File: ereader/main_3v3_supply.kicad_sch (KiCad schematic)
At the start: 20 parts, among them Q3 DMN2056U-7, U13 TPS63806YFFR, U16 74LVC1G17GW,125

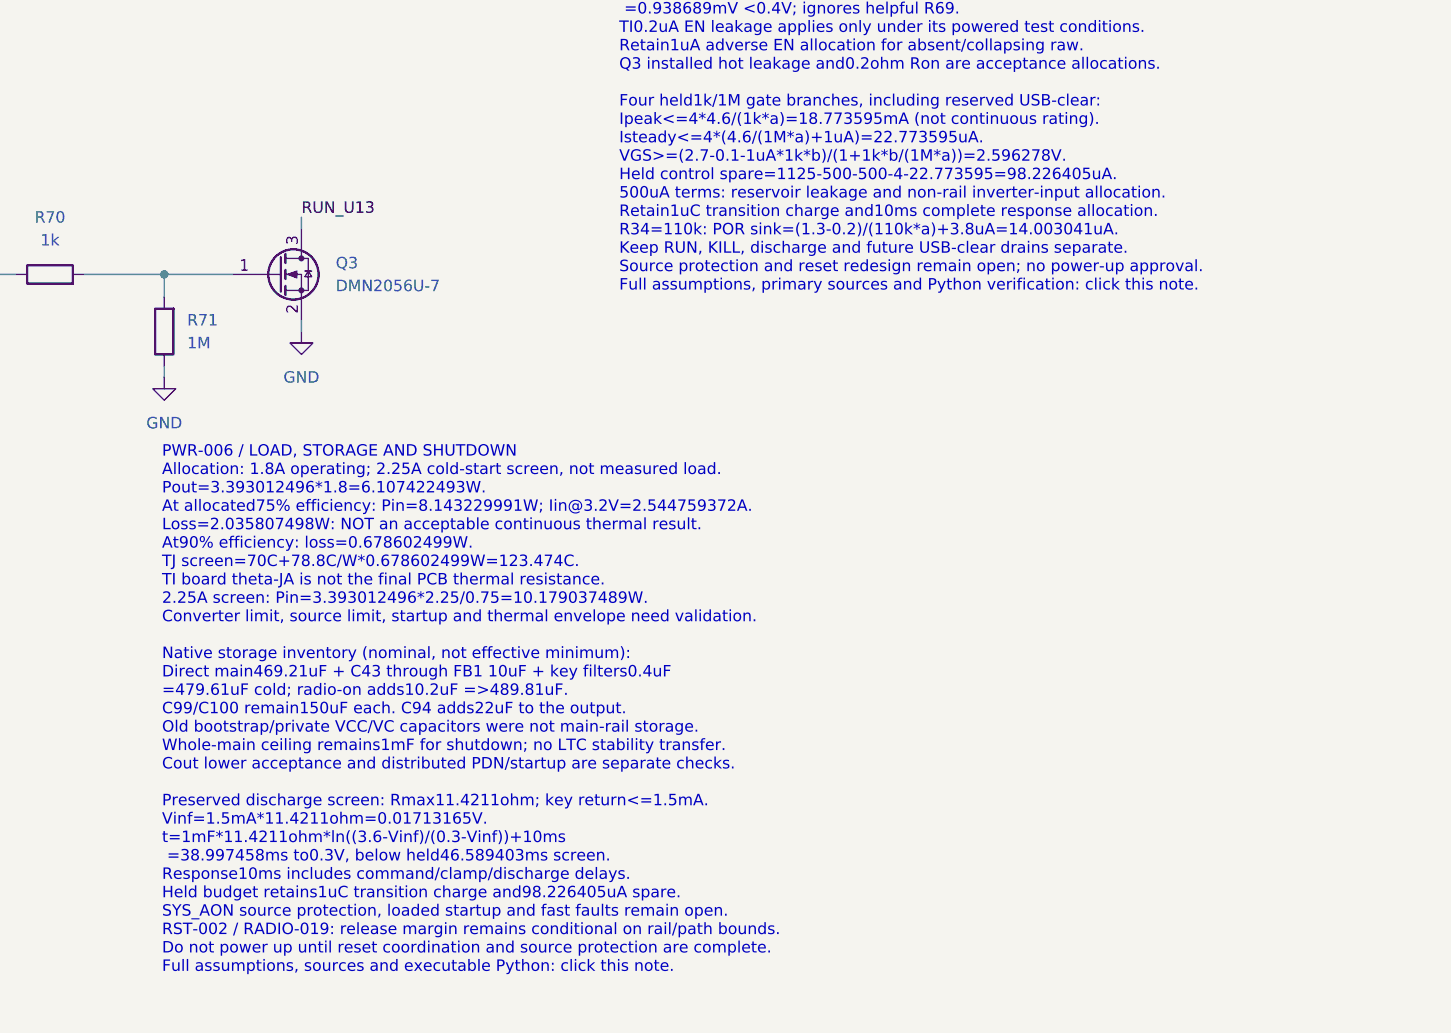
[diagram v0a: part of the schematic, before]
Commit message: WIP: integrate orientation sensor and refresh schematic review exports
Add LIS2DW12 host wiring and sourced passives, revise held-supply discharge calculations, document camera and capacitance screens, and refresh standard capacitor caches. Include reviewed 14-page PDF and reconciled native BOM. ERC remains 111 errors and 11 warnings; electrical design is incomplete. Refs #21.
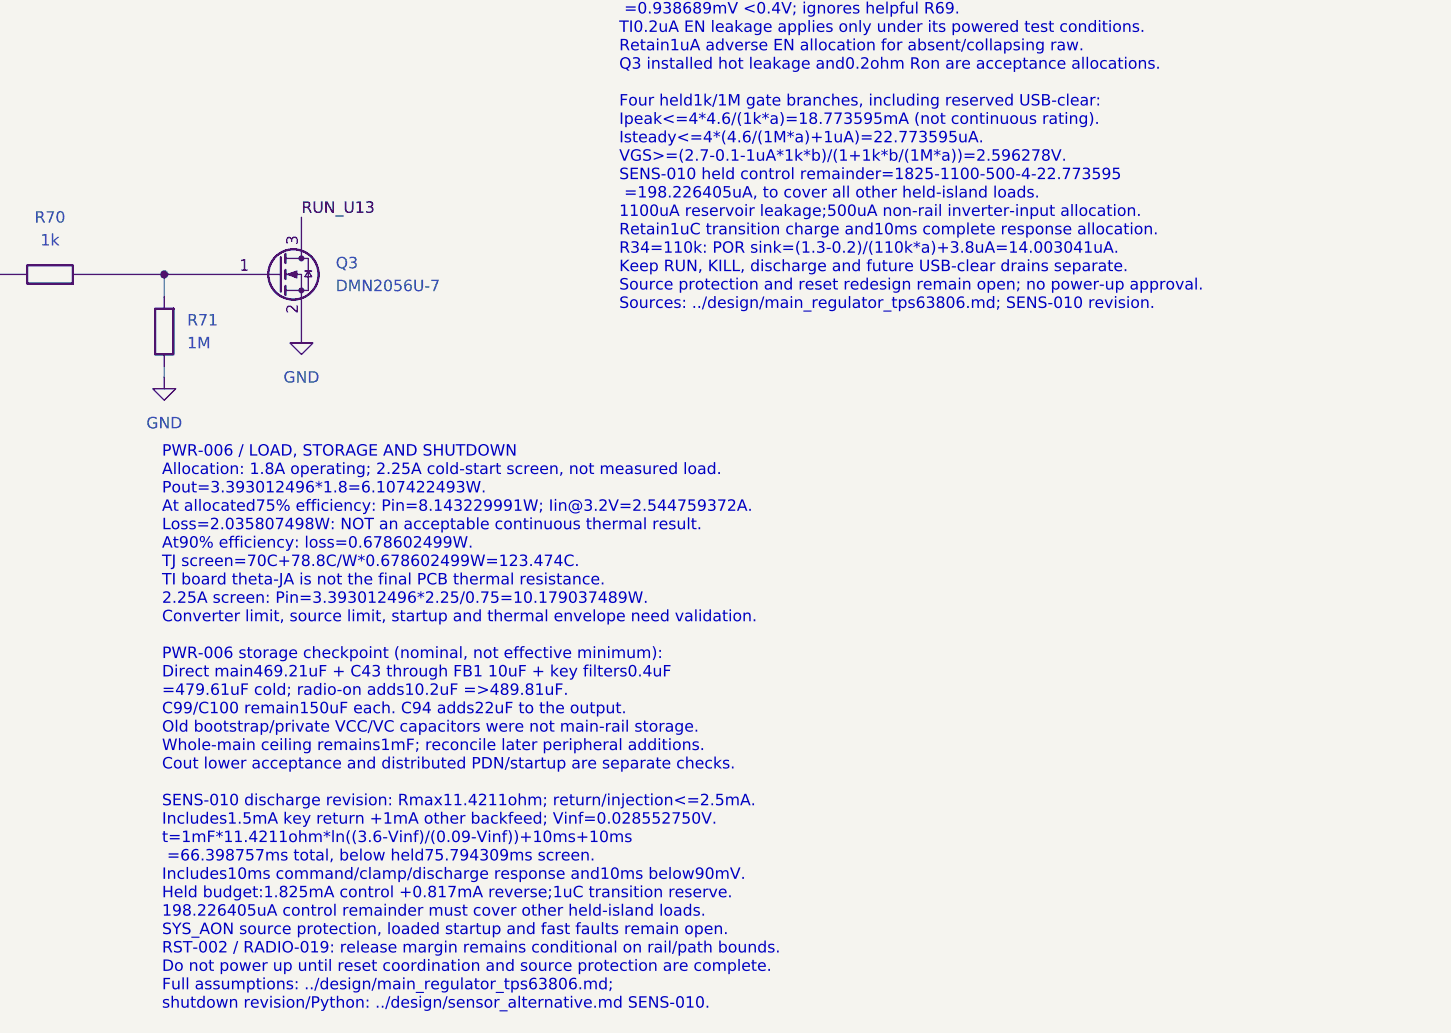
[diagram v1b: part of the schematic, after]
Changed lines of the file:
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@@
 		(rev "0.3 DRAFT")
 	)
-	(text "PWR-006 / LOAD, STORAGE AND SHUTDOWN\nAllocation: 1.8A operating; 2.25A cold-start screen, not measured load.\nPout=3.393012496*1.8=6.107422493W.\nAt allocated75% efficiency: Pin=8.143229991W; Iin@3.2V=2.544759372A.\nLoss=2.035807498W: NOT an acceptable continuous thermal result.\nAt90% efficiency: loss=0.678602499W.\nTJ screen=70C+78.8C/W*0.678602499W=123.474C.\nTI board theta-JA is not the final PCB thermal resistance.\n2.25A screen: Pin=3.393012496*2.25/0.75=10.179037489W.\nConverter limit, source limit, startup and thermal envelope need validation.\n\nNative storage inventory (nominal, not effective minimum):\nDirect main469.21uF + C43 through FB1 10uF + key filters0.4uF\n=479.61uF cold; radio-on adds10.2uF =>489.81uF.\nC99/C100 remain150uF each. C94 adds22uF to the output.\nOld bootstrap/private VCC/VC capacitors were not main-rail storage.\nWhole-main ceiling remains1mF for shutdown; no LTC stability transfer.\nCout lower acceptance and distributed PDN/startup are separate checks.\n\nPreserved discharge screen: Rmax11.4211ohm; key return<=1.5mA.\nVinf=1.5mA*11.4211ohm=0.01713165V.\nt=1mF*11.4211ohm*ln((3.6-Vinf)/(0.3-Vinf))+10ms\n =38.997458ms to0.3V, below held46.589403ms screen.\nResponse10ms includes command/clamp/discharge delays.\nHeld budget retains1uC transition charge and98.226405uA spare.\nSYS_AON source protection, loaded startup and fast faults remain open.\nRST-002 / RADIO-019: release margin remains conditional on rail/path bounds.\nDo not power up until reset coordination and source protection are complete.\nFull assumptions, sources and executable Python: click this note."
+	(text "PWR-006 / LOAD, STORAGE AND SHUTDOWN\nAllocation: 1.8A operating; 2.25A cold-start screen, not measured load.\nPout=3.393012496*1.8=6.107422493W.\nAt allocated75% efficiency: Pin=8.143229991W; Iin@3.2V=2.544759372A.\nLoss=2.035807498W: NOT an acceptable continuous thermal result.\nAt90% efficiency: loss=0.678602499W.\nTJ screen=70C+78.8C/W*0.678602499W=123.474C.\nTI board theta-JA is not the final PCB thermal resistance.\n2.25A screen: Pin=3.393012496*2.25/0.75=10.179037489W.\nConverter limit, source limit, startup and thermal envelope need validation.\n\nPWR-006 storage checkpoint (nominal, not effective minimum):\nDirect main469.21uF + C43 through FB1 10uF + key filters0.4uF\n=479.61uF cold; radio-on adds10.2uF =>489.81uF.\nC99/C100 remain150uF each. C94 adds22uF to the output.\nOld bootstrap/private VCC/VC capacitors were not main-rail storage.\nWhole-main ceiling remains1mF; reconcile later peripheral additions.\nCout lower acceptance and distributed PDN/startup are separate checks.\n\nSENS-010 discharge revision: Rmax11.4211ohm; return/injection<=2.5mA.\nIncludes1.5mA key return +1mA other backfeed; Vinf=0.028552750V.\nt=1mF*11.4211ohm*ln((3.6-Vinf)/(0.09-Vinf))+10ms+10ms\n =66.398757ms total, below held75.794309ms screen.\nIncludes10ms command/clamp/discharge response and10ms below90mV.\nHeld budget:1.825mA control +0.817mA reverse;1uC transition reserve.\n198.226405uA control remainder must cover other held-island loads.\nSYS_AON source protection, loaded startup and fast faults remain open.\nRST-002 / RADIO-019: release margin remains conditional on rail/path bounds.\nDo not power up until reset coordination and source protection are complete.\nFull assumptions: ../design/main_regulator_tps63806.md;\nshutdown revision/Python: ../design/sensor_alternative.md SENS-010."
 		(exclude_from_sim no)
 		(at 215.646 190.5 0)
@@
 			)
 			(justify left top)
-			(href "https://github.com/bsikar/ra8-firmware/blob/design/ereader-circuit/ra8p1_kicad/design/main_regulator_tps63806.md")
+			(href "https://github.com/bsikar/ra8p1-ereader-kicad/blob/main/design/main_regulator_tps63806.md")
 		)
 	)
-	(text "PWR-006 / HELD ENABLE AND SHUTDOWN CLAMP\nU16 buffers MAIN_PWR_EN; Q3 independently clamps EN during raw collapse.\nRUN_U13 is the preserved control net; U13 pin A1 is now EN.\nEN VIH>=1.2V; VIL<=0.4V. MODE tied to VIN selects forced PWM.\na=0.99*0.99=0.9801; b=1.01*1.01=1.0201 resistor factors.\nENhigh>=(3.2-0.1-1.2uA*1k*b)/(1+1k*b/(68k*a))\n =3.052060850V >1.2V. Includes allocated1uA Q3 off leakage.\nU16 high load<=4.6/(68k*a)+1.2uA=70.220568uA <100uA.\nENlow<=0.1+0.2uA*1k*b=0.100204020V <0.4V.\nAt zero raw: EN<=(2uA+1uA)*68k*b=0.208100400V.\nZero-raw screen uses U16 Ioff; not the intervening undefined region.\nHeld Q3: EN<=(4.6/(1k*a)+1uA)/(1/(1k*a)+1/0.2ohm)\n =0.938689mV <0.4V; ignores helpful R69.\nTI0.2uA EN leakage applies only under its powered test conditions.\nRetain1uA adverse EN allocation for absent/collapsing raw.\nQ3 installed hot leakage and0.2ohm Ron are acceptance allocations.\n\nFour held1k/1M gate branches, including reserved USB-clear:\nIpeak<=4*4.6/(1k*a)=18.773595mA (not continuous rating).\nIsteady<=4*(4.6/(1M*a)+1uA)=22.773595uA.\nVGS>=(2.7-0.1-1uA*1k*b)/(1+1k*b/(1M*a))=2.596278V.\nHeld control spare=1125-500-500-4-22.773595=98.226405uA.\n500uA terms: reservoir leakage and non-rail inverter-input allocation.\nRetain1uC transition charge and10ms complete response allocation.\nR34=110k: POR sink=(1.3-0.2)/(110k*a)+3.8uA=14.003041uA.\nKeep RUN, KILL, discharge and future USB-clear drains separate.\nSource protection and reset redesign remain open; no power-up approval.\nFull assumptions, primary sources and Python verification: click this note."
+	(text "PWR-006 / HELD ENABLE AND SHUTDOWN CLAMP\nU16 buffers MAIN_PWR_EN; Q3 independently clamps EN during raw collapse.\nRUN_U13 is the preserved control net; U13 pin A1 is now EN.\nEN VIH>=1.2V; VIL<=0.4V. MODE tied to VIN selects forced PWM.\na=0.99*0.99=0.9801; b=1.01*1.01=1.0201 resistor factors.\nENhigh>=(3.2-0.1-1.2uA*1k*b)/(1+1k*b/(68k*a))\n =3.052060850V >1.2V. Includes allocated1uA Q3 off leakage.\nU16 high load<=4.6/(68k*a)+1.2uA=70.220568uA <100uA.\nENlow<=0.1+0.2uA*1k*b=0.100204020V <0.4V.\nAt zero raw: EN<=(2uA+1uA)*68k*b=0.208100400V.\nZero-raw screen uses U16 Ioff; not the intervening undefined region.\nHeld Q3: EN<=(4.6/(1k*a)+1uA)/(1/(1k*a)+1/0.2ohm)\n =0.938689mV <0.4V; ignores helpful R69.\nTI0.2uA EN leakage applies only under its powered test conditions.\nRetain1uA adverse EN allocation for absent/collapsing raw.\nQ3 installed hot leakage and0.2ohm Ron are acceptance allocations.\n\nFour held1k/1M gate branches, including reserved USB-clear:\nIpeak<=4*4.6/(1k*a)=18.773595mA (not continuous rating).\nIsteady<=4*(4.6/(1M*a)+1uA)=22.773595uA.\nVGS>=(2.7-0.1-1uA*1k*b)/(1+1k*b/(1M*a))=2.596278V.\nSENS-010 held control remainder=1825-1100-500-4-22.773595\n =198.226405uA, to cover all other held-island loads.\n1100uA reservoir leakage;500uA non-rail inverter-input allocation.\nRetain1uC transition charge and10ms complete response allocation.\nR34=110k: POR sink=(1.3-0.2)/(110k*a)+3.8uA=14.003041uA.\nKeep RUN, KILL, discharge and future USB-clear drains separate.\nSource protection and reset redesign remain open; no power-up approval.\nSources: ../design/main_regulator_tps63806.md; SENS-010 revision."
 		(exclude_from_sim no)
 		(at 266.446 116.84 0)
@@
 			)
 			(justify left top)
-			(href "https://github.com/bsikar/ra8-firmware/blob/design/ereader-circuit/ra8p1_kicad/design/main_regulator_tps63806.md")
+			(href "https://github.com/bsikar/ra8p1-ereader-kicad/blob/main/design/main_regulator_tps63806.md")
 		)
 	)
